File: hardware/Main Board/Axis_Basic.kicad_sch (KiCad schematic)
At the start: 76 parts, among them J1 USB4105-GF-A, J2 JST_PH, J3 JST_SH, J4 JST_SH, J5 S2B-PH-K-S, J6 1-84952-4, SW1 RKB2SJK, SW2 RKB2SJK, U1 TLV493D, U2 UA78M33CDCYR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

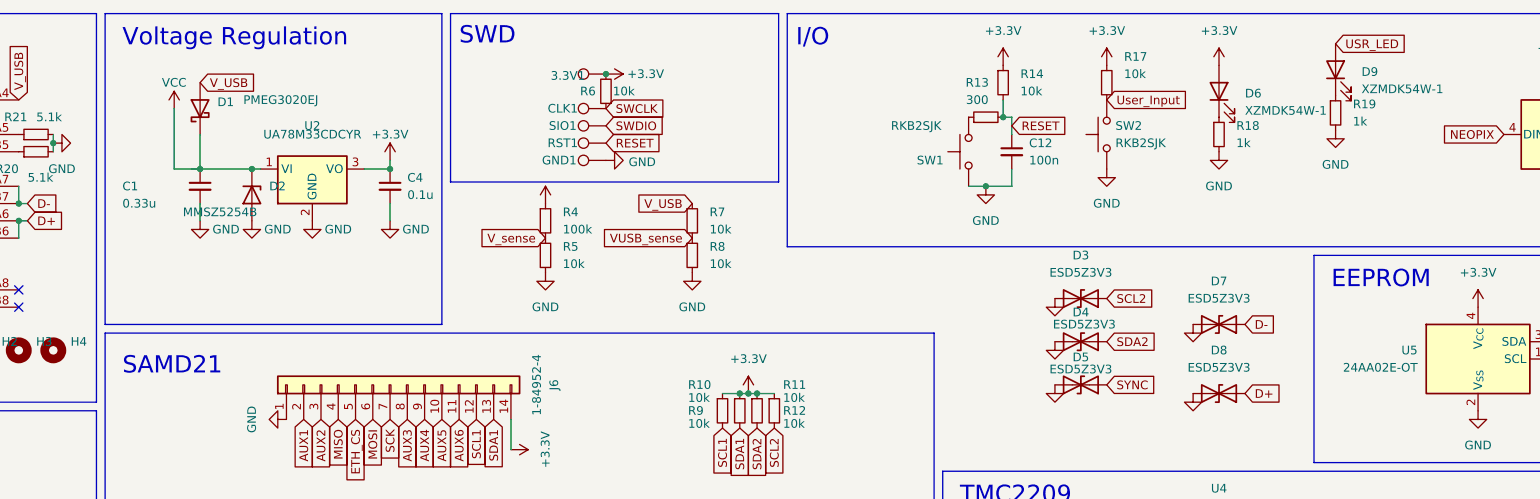
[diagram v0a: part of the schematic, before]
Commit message: Fix resistor values
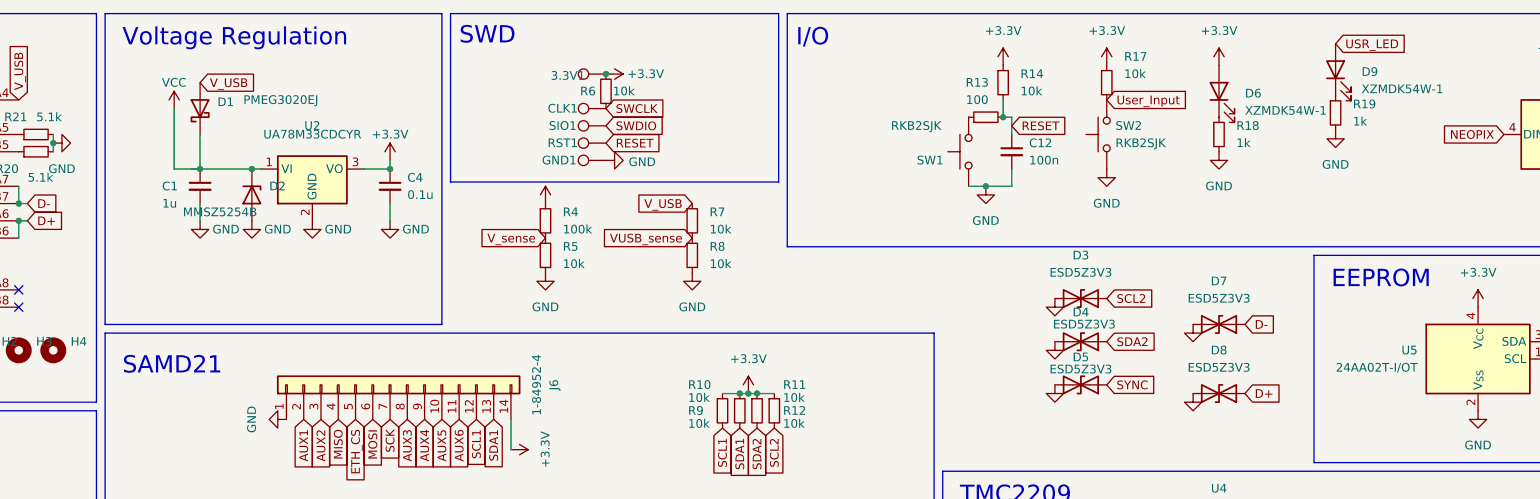
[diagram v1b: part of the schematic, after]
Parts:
- C1: value 0.33u -> 1u
- R13: value 300 -> 100
- U5: value 24AA02E-OT -> 24AA02T-I/OT
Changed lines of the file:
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@@
 			)
 		)
-		(property "Value" "24AA02E-OT"
+		(property "Value" "24AA02T-I/OT"
 			(at 246.38 66.0399 0)
 			(effects
@@
 		(dnp no)
 		(property "Reference" "C1"
-			(at 55.88 39.37 0)
+			(at 61.722 39.37 0)
 			(effects
 				(font
@@
 			)
 		)
-		(property "Value" "0.33u"
-			(at 55.88 41.91 0)
+		(property "Value" "1u"
+			(at 61.722 41.91 0)
 			(effects
 				(font
@@
 			)
 		)
-		(property "Value" "300"
+		(property "Value" "100"
 			(at 181.61 26.67 90)
 			(effects

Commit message: EthernetHat ordered
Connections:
- net USR_LED: now also U3.28 (PB15/S4.3); no longer U3.26 (PB13/S4.1)
- no-connect marks 19 -> 18
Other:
- note added: "SAMD51"
- note removed: "SAMD21"
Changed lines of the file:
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@@
-	)
-	(no_connect
-		(at 87.63 180.34)
 	)
 	(no_connect
@@
 		)
 	)
-	(text "SAMD21"
+	(text "SAMD51"
 		(exclude_from_sim no)
 		(at 55.88 67.31 0)
@@
 	(global_label "USR_LED"
 		(shape input)
-		(at 87.63 175.26 180)
-		(fields_autoplaced yes)
-		(effects
-			(font
-				(size 1.27 1.27)
-			)
-			(justify right)
-		)
-		(property "Intersheetrefs" "${INTERSHEET_REFS}"
-			(at 76.4201 175.26 0)
-			(effects
-				(font
+		(at 87.63 180.34 180)
+		(fields_autoplaced yes)
+		(effects
+			(font
+				(size 1.27 1.27)
+			)
+			(justify right)
+		)
+		(property "Intersheetrefs" "${INTERSHEET_REFS}"
+			(at 76.4201 180.34 0)
+			(effects
+				(font

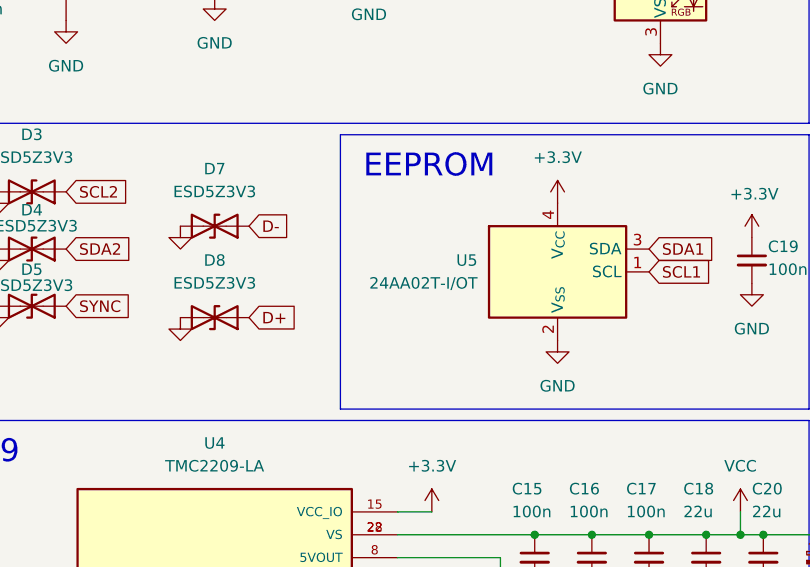
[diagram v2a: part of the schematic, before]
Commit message: Update flash part number
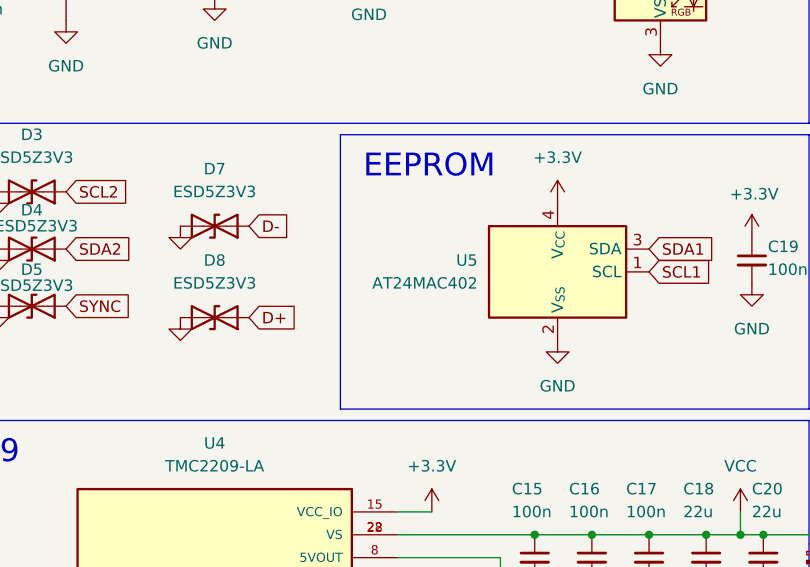
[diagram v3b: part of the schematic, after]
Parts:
- D2: value MMSZ5254B -> MMSZ5254B
- U5: value 24AA02T-I/OT -> AT24MAC402
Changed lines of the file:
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@@
 			)
 		)
-		(property "Value" "24AA02T-I/OT"
+		(property "Value" "AT24MAC402"
 			(at 246.38 66.0399 0)
 			(effects
@@
 			)
 		)
-		(property "Value" "	MMSZ5254B"
+		(property "Value" "MMSZ5254B"
 			(at 64.77 43.18 90)
 			(effects
